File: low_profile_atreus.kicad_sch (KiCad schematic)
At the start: 14 parts, among them J1 Conn_02x03_Odd_Even, J3 USB_C_Receptacle, U3 ATmega32U4-A, Y1 Crystal

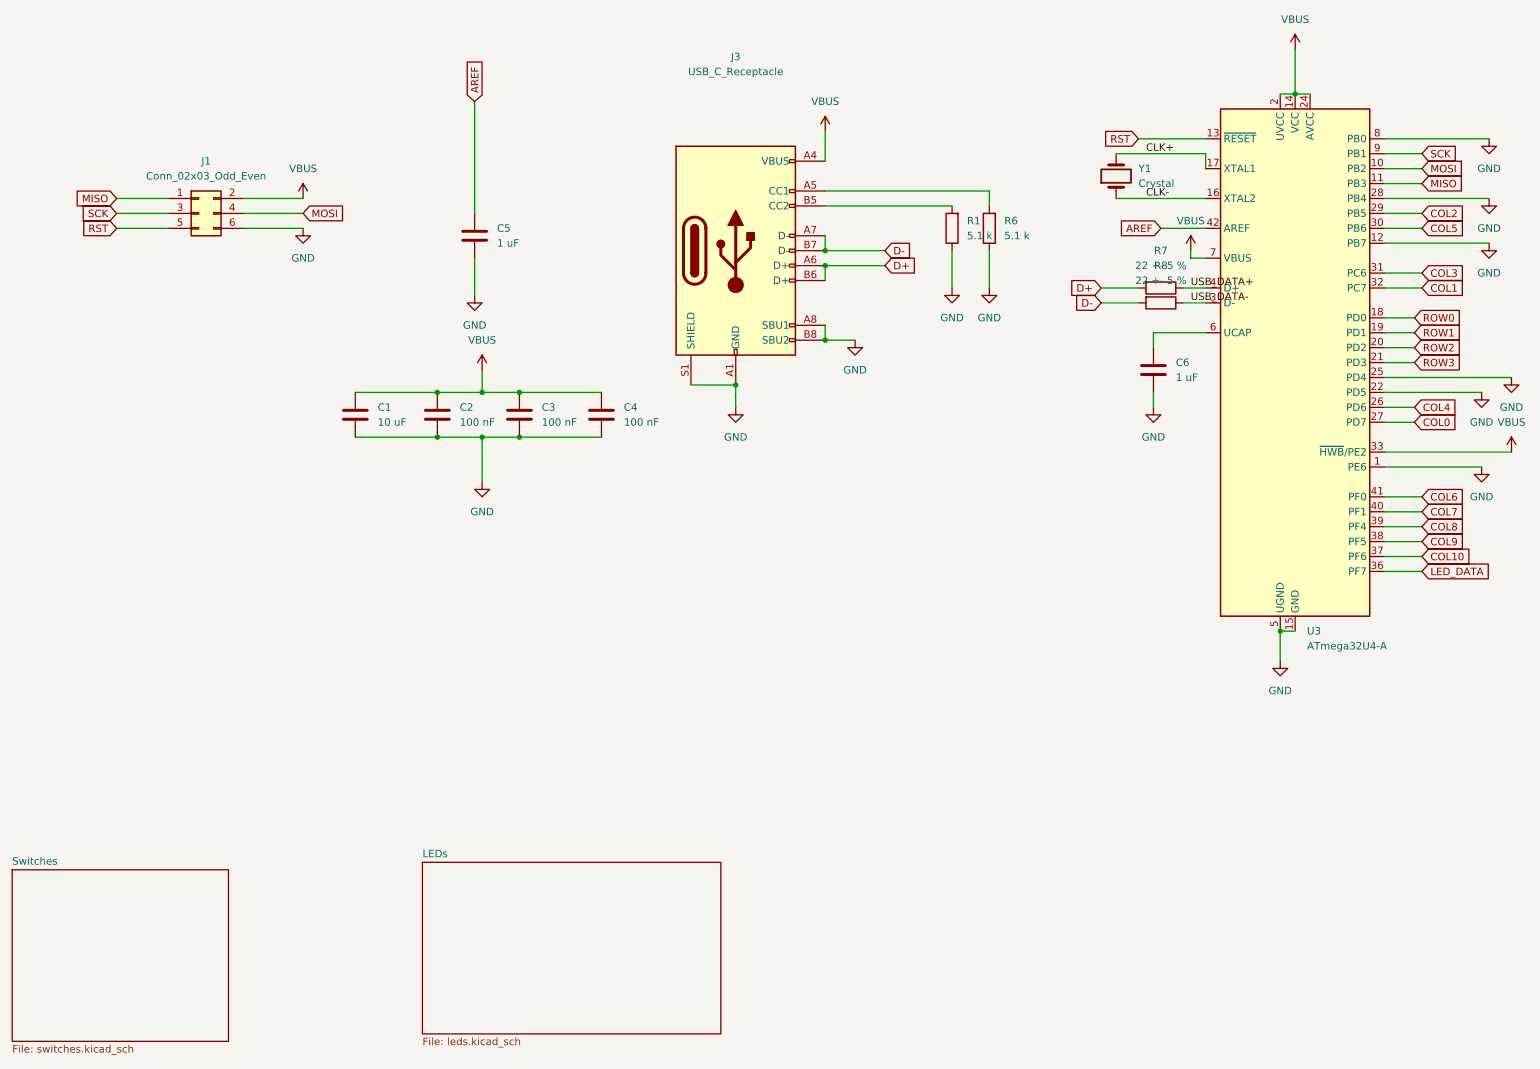
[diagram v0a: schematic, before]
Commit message: Atreus Low Profile PCB Version 1.0.0
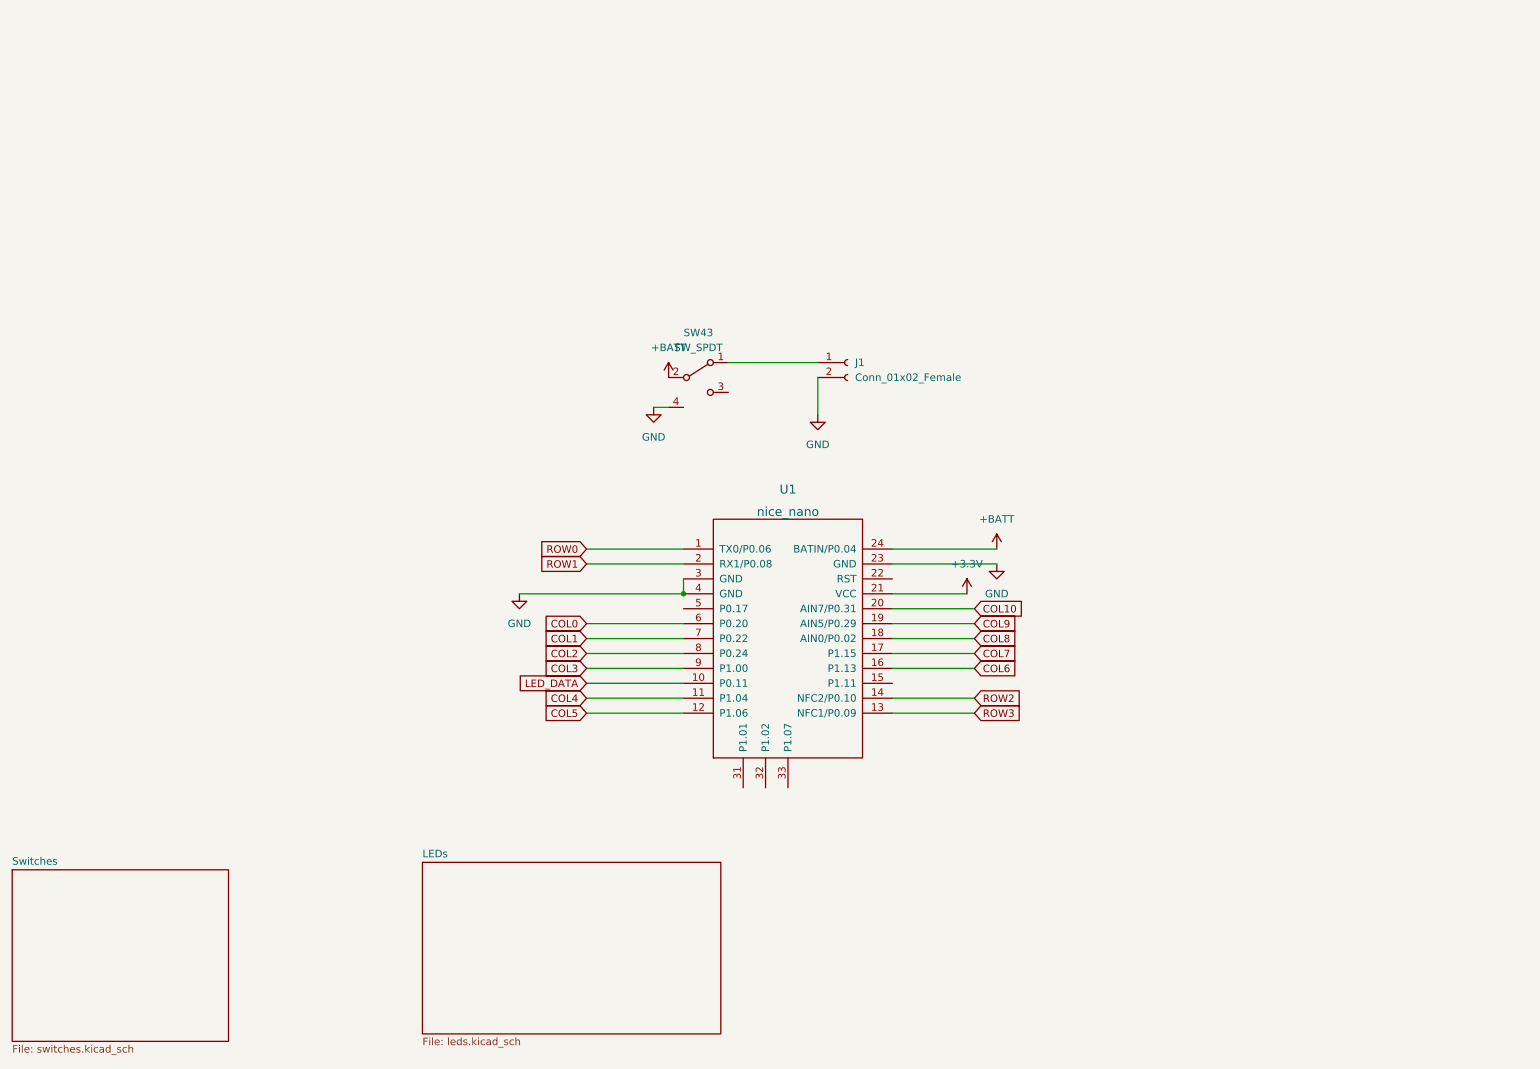
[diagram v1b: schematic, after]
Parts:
- removed C1: 10 uF, Capacitor_SMD:C_1210_3225Metric_Pad1.33x2.70mm_HandSolder, symbol Device:C
- removed C2, C3, C4: 100 nF, Capacitor_SMD:C_1210_3225Metric_Pad1.33x2.70mm_HandSolder, symbol Device:C
- removed C5, C6: 1 uF, Capacitor_SMD:C_1210_3225Metric_Pad1.33x2.70mm_HandSolder, symbol Device:C
- removed J1: Conn_02x03_Odd_Even, Connector_PinHeader_2.54mm:PinHeader_2x03_P2.54mm_Vertical_SMD, symbol Connector_Generic:Conn_02x03_Odd_Even
- removed J3: USB_C_Receptacle, Connector_USB:USB_C_Receptacle_GCT_USB4085, symbol Connector:USB_C_Receptacle_USB2.0
- removed R1, R6: 5.1 k, Resistor_SMD:R_1210_3225Metric_Pad1.30x2.65mm_HandSolder, symbol Device:R
- removed R7, R8: 22 +- 5 %, Resistor_SMD:R_1210_3225Metric_Pad1.30x2.65mm_HandSolder, symbol Device:R
- removed U3: ATmega32U4-A, Package_QFP:TQFP-44_10x10mm_P0.8mm, symbol MCU_Microchip_ATmega:ATmega32U4-A
- removed Y1: Crystal, Crystal:Crystal_SMD_Abracon_ABM3-2Pin_5.0x3.2mm_HandSoldering, symbol Device:Crystal
- added J1: Conn_01x02_Female, Connector_JST:JST_PH_S2B-PH-K_1x02_P2.00mm_Horizontal, symbol Connector:Conn_01x02_Female
- added SW43: SW_SPDT, VoidSwitch:MSK12C02, symbol voidswitch:SW_SPDT
- added U1: nice_nano, nice-nano-kicad-master:nice_nano, symbol nice!nano:nice_nano
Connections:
- net COL0: now also U1.6 (P0.20)
- net COL1: now also U1.7 (P0.22)
- net COL10: now also U1.20 (AIN7/P0.31)
- net COL2: now also U1.8 (P0.24)
- net COL3: now also U1.9 (P1.00)
- net COL4: now also U1.11 (P1.04)
- net COL5: now also U1.12 (P1.06)
- net COL6: now also U1.16 (P1.13)
- net COL7: now also U1.17 (P1.15)
- net COL8: now also U1.18 (AIN0/P0.02)
- net COL9: now also U1.19 (AIN5/P0.29)
- net GND: now also J1.2 (Pin_2), SW43.4 (GND), U1.23 (GND), U1.3 (GND), U1.4 (GND)
- net LED_DATA: now also U1.10 (P0.11)
- net ROW0: now also U1.1 (TX0/P0.06)
- net ROW1: now also U1.2 (RX1/P0.08)
- net ROW2: now also U1.14 (NFC2/P0.10)
- net ROW3: now also U1.13 (NFC1/P0.09)
- new net: J1.1 (Pin_1), SW43.1 (A)
- new net +3V3: U1.21 (VCC)
- new net +BATT: SW43.2 (B), U1.24 (BATIN/P0.04)
